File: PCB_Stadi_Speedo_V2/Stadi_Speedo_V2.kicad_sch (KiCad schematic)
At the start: 79 parts, among them J1 USB_B_Micro, J2 OLED I2C, J3 ICSP, J4 OLED SH1106, J5 SPÍD & PWR, J6 AUX DDAA, J7 ENG RPM, Q1 140817143200, Q2 PC817, U1 Mikroprofesor, U2 FT232RL, U3 LM1117MP-5.0, U4 ME6211C33M5, Y1 16MHz

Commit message: PCB V2 Update
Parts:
- added C32, C34: 100n, Capacitor_SMD:C_0603_1608Metric, symbol Device:C_Small
- added C33: 1u, Capacitor_SMD:C_0603_1608Metric, symbol Device:C_Small
- added R19, R23: 10K, Resistor_SMD:R_0603_1608Metric, symbol Device:R_Small
- added R21, R22: 20K, Resistor_SMD:R_0603_1608Metric, symbol Device:R_Small
- added U5: MAX31855KASA, Package_SO:SOIC-8_3.9x4.9mm_P1.27mm, symbol Sensor_Temperature:MAX31855KASA
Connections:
- net +3V3: now also C32.2, C33.2, U5.4 (V_{CC})
- net GND: now also J4.30 (Pin_30), C32.1, C33.1, R21.1, R22.1, U5.1 (GND)
- net VCC: no longer C26.2, C27.2, J4.28 (Pin_28)
- net D6/CS K: now reaches U1.10 (PD6)
- net D6/CS K: now also R23.2
- net D7/SCK K: now reaches U1.11 (PD7)
- net D7/SCK K: now also R19.2
- net D8/SO K: now reaches U1.12 (PB0)
- net D8/SO K: now also U5.7 (SO)
- new net: R19.1, R21.2, U5.5 (SCK)
- new net: R22.2, R23.1, U5.6 (~{CS})
- new net OLED VCC: C26.2, C27.2, J4.28 (Pin_28)
- new net T+: C34.2, U5.3 (T+)
- new net T-: C34.1, U5.2 (T-)
- no-connect marks 22 -> 19
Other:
- note added: "MAXík (optional)"
- moved on the sheet: U1

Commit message: BUCK KONVERTER ADD
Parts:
- removed U3: LM1117MP-5.0, Package_TO_SOT_SMD:SOT-223-3_TabPin2, symbol Regulator_Linear:LM1117MP-5.0
- added C35, C36: 100n, Capacitor_SMD:C_0603_1608Metric, symbol Device:C_Small
- added L1: L_Ferrite, Inductor_SMD:L_Bourns_SRP2313AA, symbol Device:L_Ferrite
- added R24: 100k, Resistor_SMD:R_0603_1608Metric, symbol Device:R_Small
- added R25: 19.1k, Resistor_SMD:R_0603_1608Metric, symbol Device:R_Small
- added U6: LMR51610YDBVR, Package_TO_SOT_SMD:SOT-23-6, symbol Regulator_Switching:LMR51430
- C5: value 1u -> 4u7
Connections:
- net +5V: now also L1.2, R24.2
- net GND: now also C35.2, R25.1, U6.2 (GND)
- net at C5.1, D9.1 (K), FB5.2: now also C35.1, U6.4 (EN), U6.5 (VIN)
- new net: C36.1, U6.1 (CB)
- new net: C36.2, L1.1, U6.6 (SW)
- new net: R24.1, R25.2, U6.3 (FB)
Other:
- note added: "Powa2 Bang for Buck"
- note removed: "Powa"
- moved on the sheet: C10, C12, C13, C17, C18, C19, C20, C21, C22, C23, C24, C25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

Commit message: Naroutovany DCDC
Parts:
- removed C35: 100n, Capacitor_SMD:C_0603_1608Metric, symbol Device:C_Small
- added C35: 4u7_16V, AERO_Capacitor_SMD:C_0603-1206_universal_Pad1.18x1.45mm, symbol Device:C_Polarized_Small
- added C37: 4u7_16V, Capacitor_Tantalum_SMD:CP_EIA-3216-10_Kemet-I, symbol Device:C_Polarized_Small
- added TP3, TP4: Label, TestPoint:TestPoint_Pad_D1.5mm, symbol AERO_TestPoint:TestPoint_Pad_2mm
- added TP5, TP6: Label, TestPoint:TestPoint_Pad_D1.0mm, symbol AERO_TestPoint:TestPoint_Pad_2mm
- C5: footprint Capacitor_SMD:C_0603_1608Metric -> AERO_Capacitor_SMD:C_0603-1206_universal_Pad1.18x1.45mm
- D3: footprint Diode_SMD:D_SOD-123F -> AERO_Diode_SMD:D_SOD-123FL
- FB5: footprint Inductor_SMD:L_Pulse_PA4332 -> AERO_Capacitor_SMD:C_0603-1206_universal_Pad1.18x1.45mm
- FB6: footprint Inductor_SMD:L_Pulse_PA4332 -> AERO_Capacitor_SMD:C_0603-1206_universal_Pad1.33x1.80mm_HandSolder
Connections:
- net +5V: now also C35.1, C37.1
- net GND: now also C35.2, C37.2
- net sw: now reaches C36.2, L1.1, U6.6 (SW)
- net PD1: now reaches R2.1, U1.31 (PD1)
- net PD1: now also TP6.1
- net PD0: now reaches R3.1, U1.30 (PD0)
- net PD0: now also TP5.1
- net at U1.25 (PC2): now also TP4.1
- net at U1.26 (PC3): now also TP3.1
- no-connect marks 19 -> 17
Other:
- note removed: "D0"
- note removed: "D1"
- moved on the sheet: C6

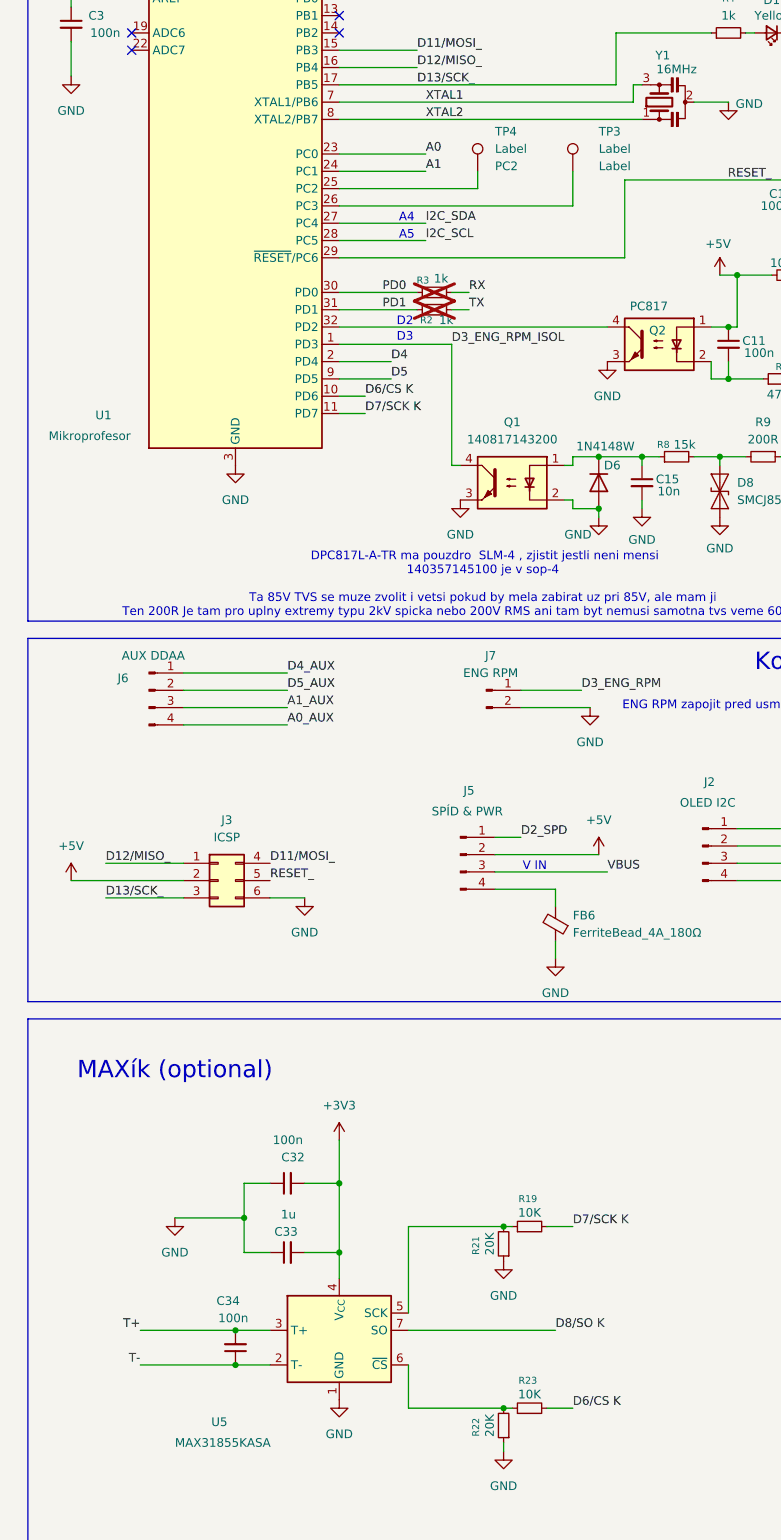
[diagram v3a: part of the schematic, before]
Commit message: pridany ferity na termistor a 5V
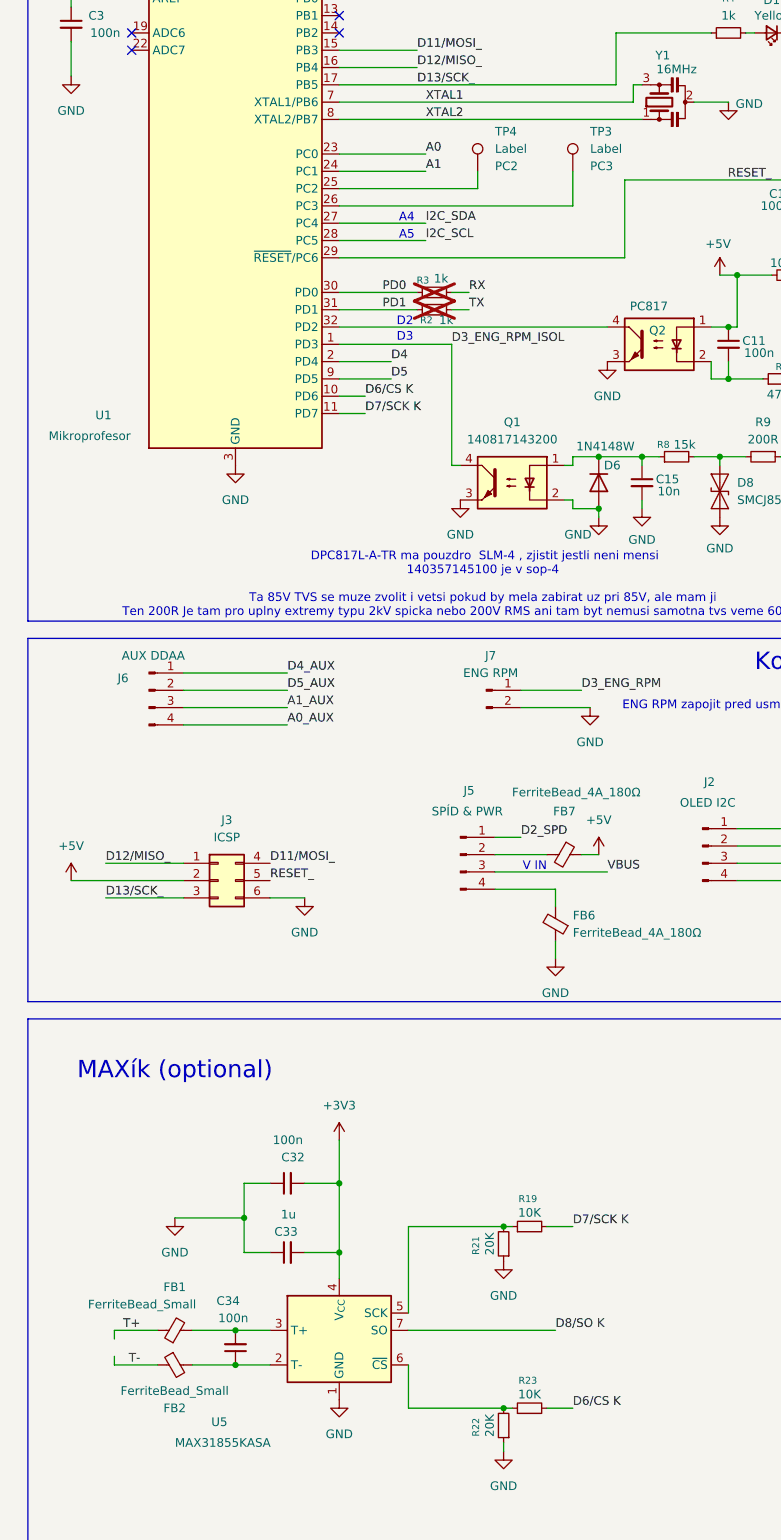
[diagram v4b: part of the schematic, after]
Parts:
- added FB1, FB2: FerriteBead_Small, Inductor_SMD:L_0603_1608Metric, symbol Device:FerriteBead_Small
- added FB7: FerriteBead_4A_180Ω, AERO_Capacitor_SMD:C_0603-1206_universal_Pad1.33x1.80mm_HandSolder, symbol AERO_FerriteBead:FerriteBead_4A_180Ohm_0806
- TP3: Label ${Value} -> PC3
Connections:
- net +5V: now also FB7.1; no longer J5.2 (Pin_2)
- net T+: now also FB1.1; no longer C34.2, U5.3 (T+)
- net T-: now also FB2.1; no longer C34.1, U5.2 (T-)
- new net: C34.1, FB2.2, U5.2 (T-)
- new net: C34.2, FB1.2, U5.3 (T+)
- new net: FB7.2, J5.2 (Pin_2)
